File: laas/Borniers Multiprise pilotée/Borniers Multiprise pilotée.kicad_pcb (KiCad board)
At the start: 2 copper layers, 170 x 40 mm, 21 parts, among them J1 Conn_02x06_Odd_Even, J2 Conn_01x02, J3 Conn_01x02, J4 Conn_01x02, J5 Conn_01x02, J6 Conn_01x02, J7 Conn_01x02

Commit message: Ajout du projet asservissement de balle en python
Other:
- board text added: "3V_1"
- board text added: "3V_2"
- board text added: "3V_3"
- board text added: "5V reversible"
- board text added: "5V_1"
- board text added: "Negative"
- board text added: "Positive"
- board text added: "Variable"
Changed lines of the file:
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@@
     (property "ki_keywords" "LED diode")
     (attr smd)
-    (fp_text reference "D2" (at 0 -1.82 90) (layer "F.SilkS")
+    (fp_text reference "D2" (at 4.01 -0.055 90) (layer "F.SilkS")
         (effects (font (size 1 1) (thickness 0.15)))
     )
@@
     (property "ki_keywords" "LED diode")
     (attr smd)
-    (fp_text reference "D6" (at 0 -1.82 90) (layer "F.SilkS")
+    (fp_text reference "D6" (at 3.95 -0.255 90) (layer "F.SilkS")
         (effects (font (size 1 1) (thickness 0.15)))
     )
@@
     (property "ki_keywords" "R res resistor")
     (attr smd)
-    (fp_text reference "R3" (at 0 -1.82 90) (layer "F.SilkS")
+    (fp_text reference "R3" (at -4.01 -0.07 90) (layer "F.SilkS")
         (effects (font (size 1 1) (thickness 0.15)))
     )
@@
     (property "ki_keywords" "LED diode")
     (attr smd)
-    (fp_text reference "D3" (at 0 -1.82 90) (layer "F.SilkS")
+    (fp_text reference "D3" (at 4.01 -0.375 90) (layer "F.SilkS")
         (effects (font (size 1 1) (thickness 0.15)))
     )
@@
     (property "ki_keywords" "R res resistor")
     (attr smd)
-    (fp_text reference "R7" (at 0 -1.82 90) (layer "F.SilkS")
+    (fp_text reference "R7" (at -4.01 0.125 90) (layer "F.SilkS")
         (effects (font (size 1 1) (thickness 0.15)))
     )
@@
     (property "ki_keywords" "R res resistor")
     (attr smd)
-    (fp_text reference "R2" (at 0 -1.82 90) (layer "F.SilkS")
+    (fp_text reference "R2" (at -4.01 -0.39 90) (layer "F.SilkS")
         (effects (font (size 1 1) (thickness 0.15)))
     )
@@
     (property "ki_keywords" "R res resistor")
     (attr smd)
-    (fp_text reference "R6" (at 0 -1.82 90) (layer "F.SilkS")
+    (fp_text reference "R6" (at -3.95 -0.19 90) (layer "F.SilkS")
         (effects (font (size 1 1) (thickness 0.15)))
     )
@@
     (property "ki_keywords" "LED diode")
     (attr smd)
-    (fp_text reference "D1" (at 0 -1.82 90) (layer "F.SilkS")
+    (fp_text reference "D1" (at 4.01 -0.37 90) (layer "F.SilkS")
         (effects (font (size 1 1) (thickness 0.15)))
     )
@@
     (property "ki_keywords" "LED diode")
     (attr smd)
-    (fp_text reference "D4" (at 0 -1.82 90) (layer "F.SilkS")
+    (fp_text reference "D4" (at 4.01 0.148 90) (layer "F.SilkS")
         (effects (font (size 1 1) (thickness 0.15)))
     )
@@
     (property "ki_keywords" "LED diode")
     (attr smd)
-    (fp_text reference "D5" (at 0 -1.82 90) (layer "F.SilkS")
+    (fp_text reference "D5" (at 4.01 -0.255 90) (layer "F.SilkS")
         (effects (font (size 1 1) (thickness 0.15)))
     )
@@
     (property "ki_keywords" "LED diode")
     (attr smd)
-    (fp_text reference "D7" (at 0 -1.82 90) (layer "F.SilkS")
+    (fp_text reference "D7" (at 4.01 0.065 90) (layer "F.SilkS")
         (effects (font (size 1 1) (thickness 0.15)))
     )
@@
     (property "ki_keywords" "R res resistor")
     (attr smd)
-    (fp_text reference "R5" (at 0 -1.82 90) (layer "F.SilkS")
+    (fp_text reference "R5" (at -4.01 -0.19 90) (layer "F.SilkS")
         (effects (font (size 1 1) (thickness 0.15)))
     )
@@
     (property "ki_keywords" "R res resistor")
     (attr smd)
-    (fp_text reference "R1" (at 0 -1.82 90) (layer "F.SilkS")
+    (fp_text reference "R1" (at -4.01 -0.075 90) (layer "F.SilkS")
         (effects (font (size 1 1) (thickness 0.15)))
     )
@@
     (property "ki_keywords" "R res resistor")
     (attr smd)
-    (fp_text reference "R4" (at 0 -1.82 90) (layer "F.SilkS")
+    (fp_text reference "R4" (at -4.01 -0.085 90) (layer "F.SilkS")
         (effects (font (size 1 1) (thickness 0.15)))
     )
@@
     (effects (font (size 1.5 1.5) (thickness 0.3) bold) (justify bottom mirror))
   )
+  (gr_text "5V reversible" (at 128.27 99.06) (layer "F.SilkS")
+    (effects (font (size 1.2 1.2) (thickness 0.2) bold) (justify left bottom))
+  )
+  (gr_text "Variable" (at 110.49 99.06) (layer "F.SilkS")
+    (effects (font (size 1.2 1.2) (thickness 0.2) bold) (justify left bottom))
+  )
+  (gr_text "3V_2" (at 182.245 99.06) (layer "F.SilkS")
+    (effects (font (size 1.2 1.2) (thickness 0.2) bold) (justify left bottom))
+  )
+  (gr_text "Positive" (at 139.065 76.835) (layer "F.SilkS")
+    (effects (font (size 1.2 1.2) (thickness 0.2) bold) (justify left bottom))
+  )
+  (gr_text "Negative" (at 139.065 104.775) (layer "F.SilkS")
+    (effects (font (size 1.2 1.2) (thickness 0.2) bold) (justify left bottom))
+  )
+  (gr_text "5V_1" (at 81.915 99.06) (layer "F.SilkS")
+    (effects (font (size 1.2 1.2) (thickness 0.2) bold) (justify left bottom))
+  )
+  (gr_text "3V_3" (at 162.56 99.06) (layer "F.SilkS")
+    (effects (font (size 1.2 1.2) (thickness 0.2) bold) (justify left bottom))
+  )
+  (gr_text "3V_1" (at 201.93 99.06) (layer "F.SilkS")
+    (effects (font (size 1.2 1.2) (thickness 0.2) bold) (justify left bottom))
+  )
   (dimension (type aligned) (layer "User.2")

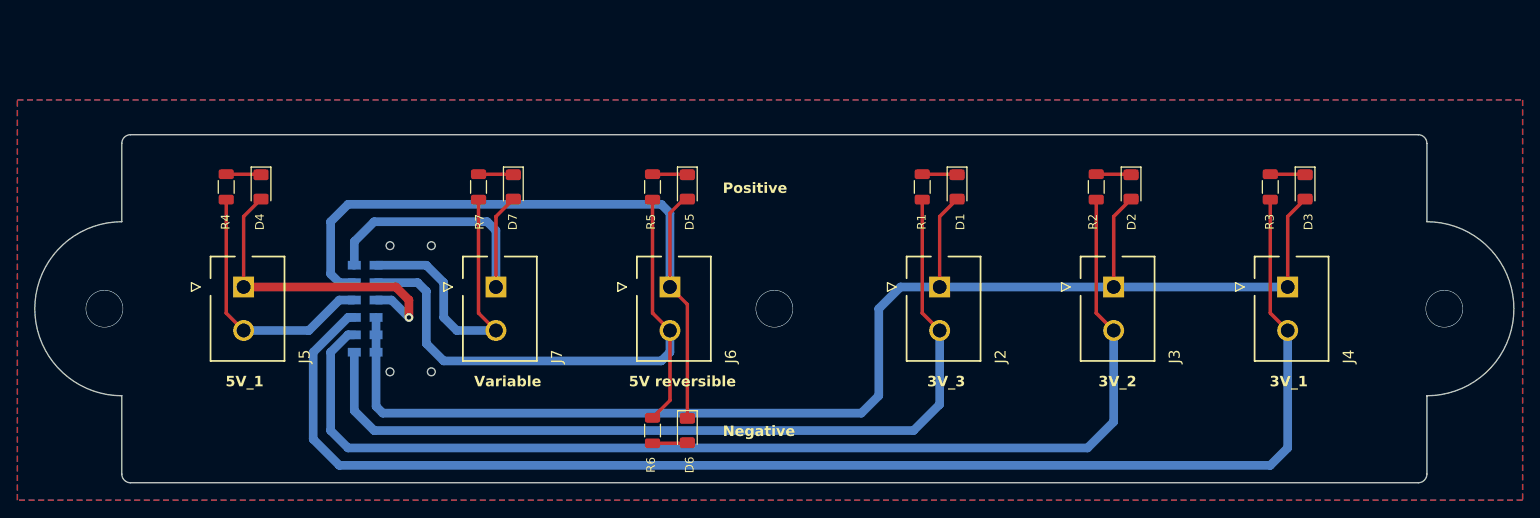
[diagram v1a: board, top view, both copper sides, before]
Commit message: Mise à jour du bornier pour la multiprise
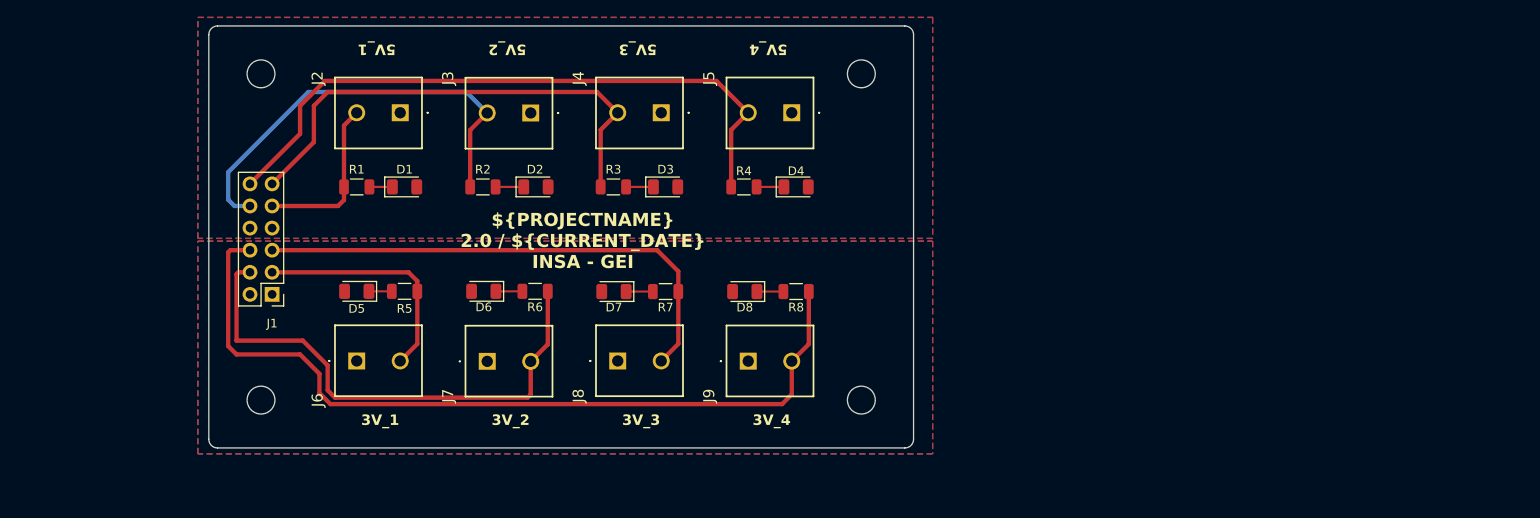
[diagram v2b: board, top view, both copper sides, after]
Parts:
- removed the D5 at (135.0, 76.0)
- removed the J6 at (133.0, 87.5)
- removed the R5 at (131.0, 76.0)
- added D4: LED, LED_SMD:LED_1206_3216Metric, F.Cu at (147.5, 76.0)
- added D8: LED, LED_SMD:LED_1206_3216Metric, F.Cu at (141.6, 88.0)
- added H1: MountingHole, MountingHole:MountingHole_3.2mm_M3, F.Cu at (86.0, 63.0)
- added H2: MountingHole, MountingHole:MountingHole_3.2mm_M3, F.Cu at (155.0, 63.0)
- added H3: MountingHole, MountingHole:MountingHole_3.2mm_M3, F.Cu at (155.0, 100.5)
- added H4: MountingHole, MountingHole:MountingHole_3.2mm_M3, F.Cu at (86.0, 100.5)
- added J5: Conn_01x02, Borniers:5442170, F.Cu at (147.0, 67.5)
- added J8: Conn_01x02, Borniers:5442170, F.Cu at (127.0, 96.0)
- added J9: Conn_01x02, Borniers:5442170, F.Cu at (142.0, 96.0)
- added R4: 1K, Resistor_SMD:R_1206_3216Metric, F.Cu at (141.5, 76.0)
- added R8: 1K, Resistor_SMD:R_1206_3216Metric, F.Cu at (147.5, 88.0)
- J1: footprint Borniers:M80-66612YY -> Connector_PinHeader_2.54mm:PinHeader_2x06_P2.54mm_Vertical; moved to F.Cu
- J2, J3, J4, J7: footprint Borniers:WR-TBL Serie 3117 - 2P -> Borniers:5442170
- J6: renamed from J5; footprint Borniers:WR-TBL Serie 3117 - 2P -> Borniers:5442170
- moved R3 75.5 mm to (126.5, 76.0), turned to 0 degrees
- moved J4 74.7 mm to (132.0, 67.5), turned to 180 degrees
- moved D3 73.5 mm to (132.5, 76.0), turned to 0 degrees
- moved R2 70.5 mm to (111.5, 76.0), turned to 0 degrees
- moved J3 69.9 mm to (117.0, 67.5), turned to 180 degrees
- moved D2 68.4 mm to (117.6, 76.0), turned to 0 degrees
- moved J2 65.2 mm to (102.0, 67.5), turned to 180 degrees
- moved R1 65.0 mm to (97.0, 76.0), turned to 0 degrees
- moved D1 63.5 mm to (102.5, 76.0), turned to 0 degrees
- moved D6 28.3 mm to (111.6, 88.0), turned to 180 degrees
- moved R7 24.6 mm to (132.5, 88.0), turned to 180 degrees
- moved R5 23.8 mm to (102.5, 88.0), turned to 180 degrees
- moved R6 20.9 mm to (117.5, 88.0), turned to 180 degrees
- moved D7 16.7 mm to (126.6, 88.0), turned to 180 degrees
- moved D5 16.3 mm to (97.0, 88.0), turned to 180 degrees
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- renumbered D4 to D5, R4 to R5
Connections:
- D6 pad 1: /PWR_+5V -> Net-(D6-K)
- D6 pad 2: Net-(D6-A) -> +5V
- D7 pad 2: /PWR_VAR_POS -> +5V
- J1 pad 1: /PWR_3V3_1 -> +5V
- J1 pad 10: +5V -> /PWR_3V3_2
- J1 pad 11: /PWR_-5V -> /PWR_3V3_3
- J1 pad 12: /PWR_VAR_NEG -> /PWR_3V3_4
- J1 pad 2: /PWR_3V3_2 -> +5V
- J1 pad 3: /PWR_3V3_3 -> /PWR_5V_1
- J1 pad 4: /PWR_5V_1 -> /PWR_5V_2
- J1 pad 5: /PWR_+5V -> /PWR_5V_3
- J1 pad 6: /PWR_VAR_POS -> /PWR_5V_4
- J1 pad 9: +3V3 -> /PWR_3V3_1
- J7 pad 1: /PWR_VAR_POS -> +5V
- J7 pad 2: /PWR_VAR_NEG -> /PWR_5V_2
- R6 pad 1: Net-(D6-A) -> /PWR_5V_2
- R6 pad 2: /PWR_-5V -> Net-(D6-K)
- R7 pad 1: /PWR_VAR_NEG -> /PWR_5V_3
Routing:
- net +3V3: track 161.2 -> 0.00 mm
- net /PWR_3V3_3: track 159.8 -> 56.9 mm
- net /PWR_5V_4: track 0.00 -> 95.3 mm
- net /PWR_+5V: track 85.0 -> 0.00 mm
- net /PWR_3V3_1: track 100.6 -> 19.2 mm
- net /PWR_3V3_2: track 131.0 -> 49.9 mm
- net /PWR_3V3_4: track 0.00 -> 74.9 mm
- net /PWR_-5V: track 70.7 -> 0.00 mm
- net /PWR_5V_2: track 0.00 -> 60.3 mm
- net /PWR_5V_3: track 0.00 -> 58.8 mm
- net /PWR_VAR_POS: track 37.8 -> 0.00 mm
- net +5V: track 37.2 -> 0.00 mm, vias 1 -> 0
- net /PWR_VAR_NEG: track 35.1 -> 0.00 mm
- net Net-(D6-A): track 4.03 -> 0.00 mm
- net Net-(D5-K) (its old number): track 4.03 -> 0.00 mm
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- added copper zone on B.Cu, net +5V
- added copper zone on F.Cu, net +5V
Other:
- board size 170 x 40 mm -> 81 x 48.5 mm
- board text added: "${PROJECTNAME} ${REVISION} / ${CURRENT_DATE} ${COMPANY}"
- board text added: "3V_4"
- board text added: "5V_2"
- board text added: "5V_3"
- board text added: "5V_4"
- board text removed: "5V reversible"
- board text removed: "Bornier Multiprise Pilotée LAAS - 2024"
- board text removed: "Negative"
- board text removed: "Positive"
- board text removed: "Variable"
